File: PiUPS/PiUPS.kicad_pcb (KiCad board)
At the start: 2 copper layers, 87.4 x 56 mm, 93 parts, among them J1 USB_C_Receptacle_USB2.0, J2 Raspberry_Pi_2_3, J3 USB_A, J4 USB_B_Micro, J5 Screw_Terminal_01x02, J6 Screw_Terminal_01x02, Q1 IRF7404, Q2 IRF7404, Q3 IRLML2803TRPBF, Q4 IRF7404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

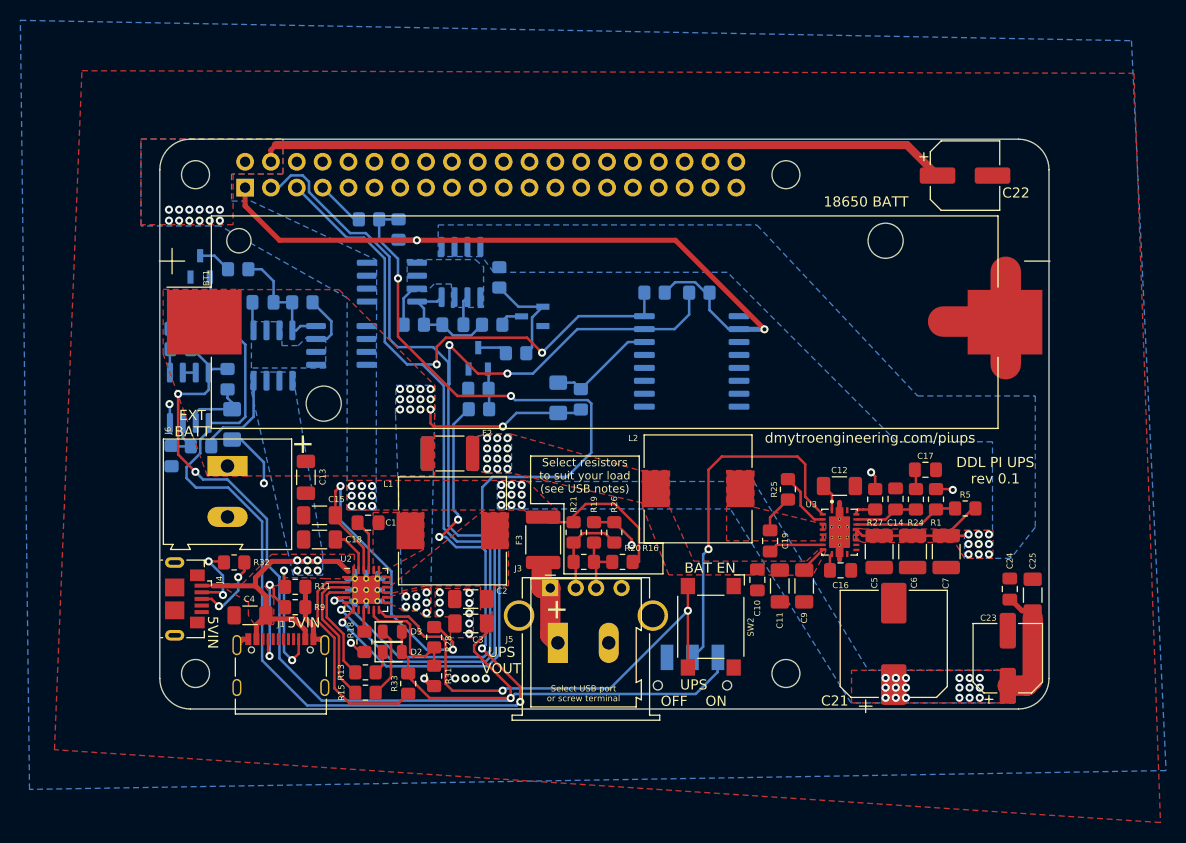
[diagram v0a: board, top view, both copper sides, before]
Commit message: Updated to include the boges to rev 0.2
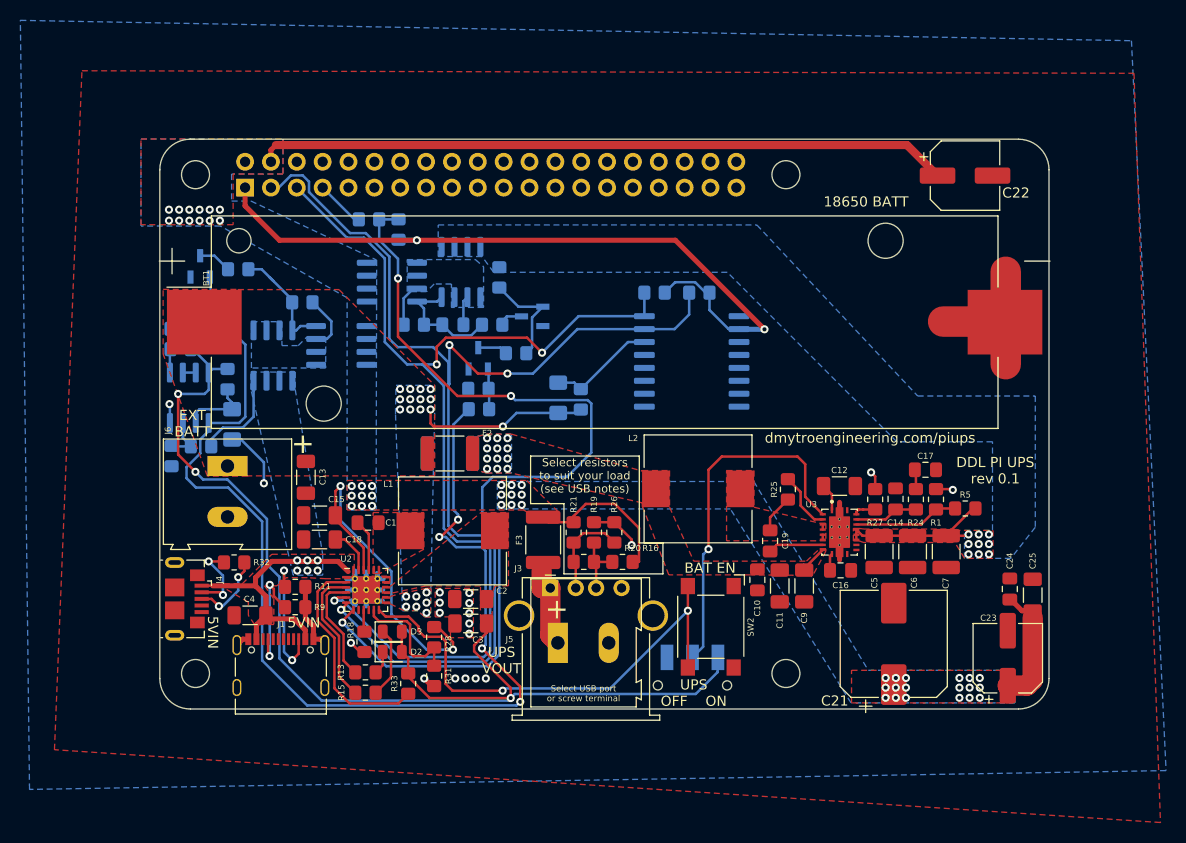
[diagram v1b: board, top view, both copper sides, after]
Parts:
- removed C8: 100nF, Capacitor_SMD:C_0805_2012Metric_Pad1.18x1.45mm_HandSolder
- R14: value 470 -> 100
- R8: value 10k -> 1k
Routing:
- net Net-(Q1-Pad1): track 8.32 -> 5.68 mm
- net Net-(Q1-Pad4): track 12.2 -> 11.7 mm
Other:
- board text added: "JLCJLCJLCJLC"

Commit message: added exprimental latching boost IC cutoff circuit + notes about dev branch file and future things to do
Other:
- board text added: "DDL PI UPS rev 0.2"
- board text removed: "DDL PI UPS rev 0.1"
- board text removed: "JLCJLCJLCJLC"

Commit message: updated to Kicad 6.0
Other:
- net class Default removed

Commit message: added label on PCB to indicate that it is outdated
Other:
- board text added: "OUTDATED PCB"
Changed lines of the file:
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@@
     (effects (font (size 1 1) (thickness 0.15)))
+  )
+  (gr_text "OUTDATED PCB" (at 104.14 53.34) (layer "Dwgs.User")
+    (effects (font (size 5 2.5) (thickness 0.3)))
   )
   (segment (start 80.7 113.4) (end 80.7 114.45) (width 0.5) (layer "F.Cu") (net 1))
